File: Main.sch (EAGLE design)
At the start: 27 parts, among them U1 L298, U2 LM 1084 IT5,0, U3 LM 1084 IT3,3, U4 L298, X1 Motors, X3 Battery

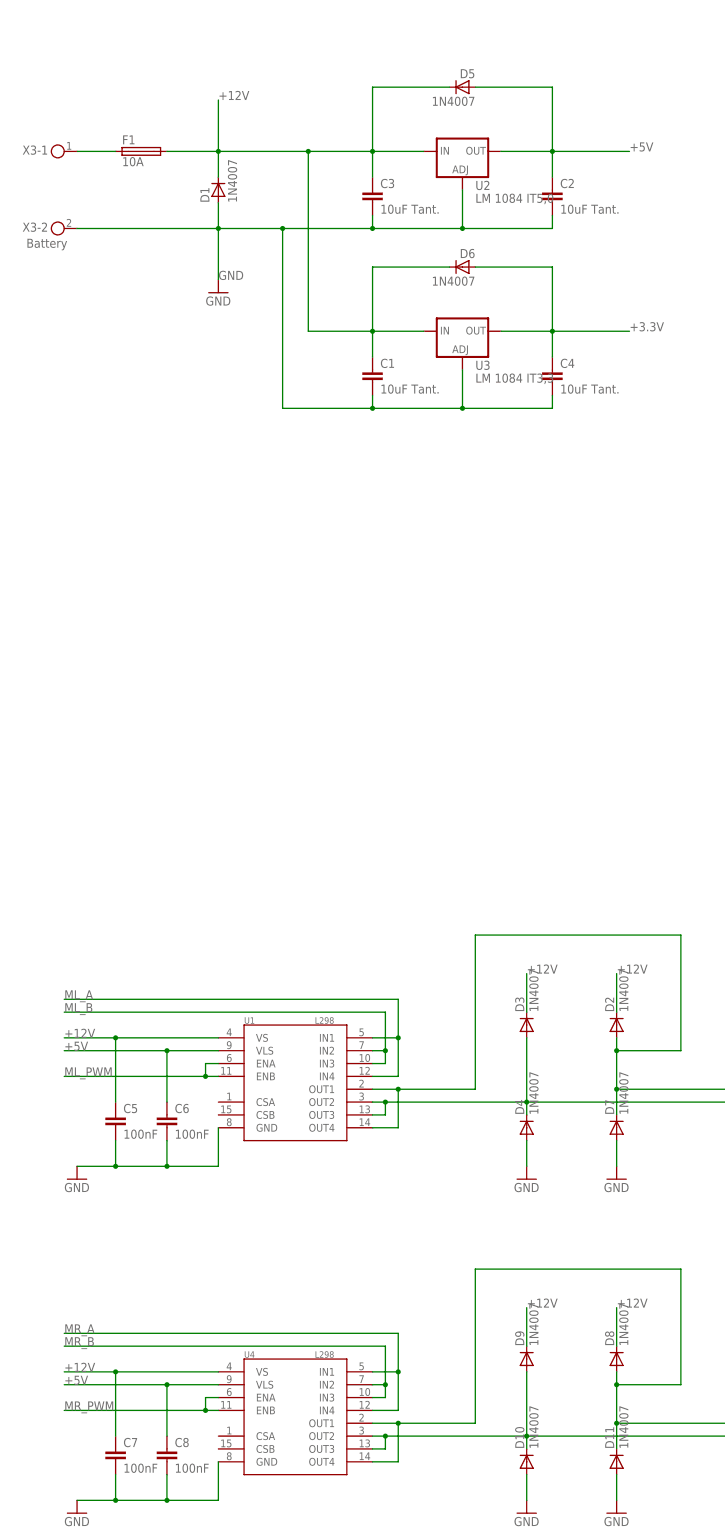
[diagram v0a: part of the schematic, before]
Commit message: better protection for reverse polarity
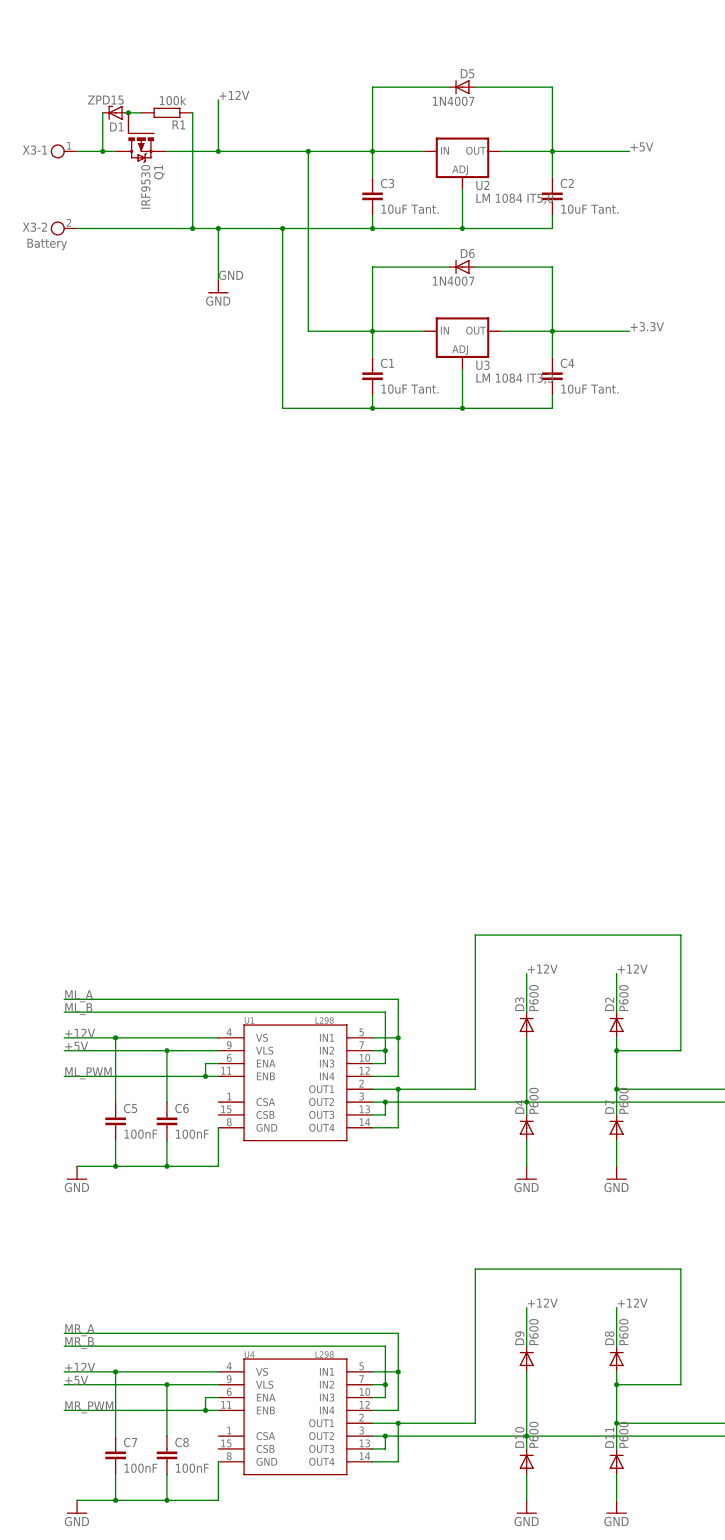
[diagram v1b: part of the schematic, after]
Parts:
- removed F1: 10A, fuse:FUSEBLANK_5X20MM
- added Q1: IRF9530, transistor-power:IRF9530
- added R1: 100k, resistor:R-EU_R0805
- D1: value 1N4007 -> ZPD15; device semicon-smd-ipc:D-MLL-41 -> diode:ZENER-DIODEDO35Z10
- D10, D11, D2, D3, D4, D7, D8, D9: value 1N4007 -> P600
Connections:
- new net N$2: D1.A, Q1.G, R1.2
- net +12V: now also Q1.S; no longer D1.C, F1.2
- net GND: now also R1.1; no longer D1.A
- net N$1: now also D1.C, Q1.D; no longer F1.1
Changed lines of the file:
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@@
 <part name="D6" library="semicon-smd-ipc" deviceset="D-" device="MLL-41" value="1N4007"/>
 <part name="C4" library="rcl" deviceset="C-EU" device="025-040X050" value="10uF Tant."/>
-<part name="D1" library="semicon-smd-ipc" deviceset="D-" device="MLL-41" value="1N4007"/>
-<part name="F1" library="fuse" deviceset="FUSE" device="BLANK_5X20MM" value="10A"/>
 <part name="FRAME1" library="frames" deviceset="DINA4_L" device="" value="Power"/>
 <part name="FRAME2" library="frames" deviceset="DINA4_L" device="" value="Motor"/>
@@
 <part name="SV1" library="con-lsta" deviceset="FE20-2" device="" value="Raspberry Pi B Plus Connector"/>
 <part name="GND4" library="supply1" deviceset="GND" device=""/>
-<part name="D2" library="diode" deviceset="P600" device="" value="1N4007"/>
-<part name="D3" library="diode" deviceset="P600" device="" value="1N4007"/>
-<part name="D4" library="diode" deviceset="P600" device="" value="1N4007"/>
-<part name="D7" library="diode" deviceset="P600" device="" value="1N4007"/>
+<part name="D2" library="diode" deviceset="P600" device="" value="P600"/>
+<part name="D3" library="diode" deviceset="P600" device="" value="P600"/>
+<part name="D4" library="diode" deviceset="P600" device="" value="P600"/>
+<part name="D7" library="diode" deviceset="P600" device="" value="P600"/>
 <part name="GND2" library="supply1" deviceset="GND" device=""/>
 <part name="GND5" library="supply1" deviceset="GND" device=""/>
@@
 <part name="C8" library="rcl" deviceset="C-EU" device="C0805" value="100nF"/>
 <part name="GND6" library="supply1" deviceset="GND" device=""/>
-<part name="D8" library="diode" deviceset="P600" device="" value="1N4007"/>
-<part name="D9" library="diode" deviceset="P600" device="" value="1N4007"/>
-<part name="D10" library="diode" deviceset="P600" device="" value="1N4007"/>
-<part name="D11" library="diode" deviceset="P600" device="" value="1N4007"/>
+<part name="D8" library="diode" deviceset="P600" device="" value="P600"/>
+<part name="D9" library="diode" deviceset="P600" device="" value="P600"/>
+<part name="D10" library="diode" deviceset="P600" device="" value="P600"/>
+<part name="D11" library="diode" deviceset="P600" device="" value="P600"/>
 <part name="GND7" library="supply1" deviceset="GND" device=""/>
 <part name="GND8" library="supply1" deviceset="GND" device=""/>
@@
 <part name="X3" library="con-ria-59" deviceset="AKL59-02" device="" value="Battery"/>
 <part name="X1" library="con-ria-59" deviceset="AKL59-08" device="" value="Motors"/>
+<part name="Q1" library="transistor-power" deviceset="IRF9530" device=""/>
+<part name="R1" library="resistor" deviceset="R-EU_" device="R0805" value="100k"/>
+<part name="D1" library="diode" deviceset="ZENER-DIODE" device="DO35Z10" value="ZPD15"/>
 </parts>
 <sheets>
@@
 <instance part="D6" gate="G$1" x="-411.48" y="317.5" rot="MR0"/>
 <instance part="C4" gate="G$1" x="-393.7" y="297.18"/>
-<instance part="D1" gate="G$1" x="-459.74" y="332.74" rot="R90"/>
-<instance part="F1" gate="G$1" x="-474.98" y="340.36"/>
 <instance part="FRAME1" gate="G$1" x="-513.08" y="213.36"/>
 <instance part="FRAME1" gate="G$2" x="-350.52" y="213.36"/>
@@
 <instance part="X1" gate="-7" x="-327.66" y="109.22"/>
 <instance part="X1" gate="-8" x="-327.66" y="104.14"/>
+<instance part="Q1" gate="G$1" x="-474.98" y="342.9" rot="R270"/>
+<instance part="R1" gate="G$1" x="-469.9" y="347.98" rot="R180"/>
+<instance part="D1" gate="G$1" x="-480.06" y="347.98" rot="R180"/>
 </instances>
 <busses>
@@
 <wire x1="-441.96" y1="304.8" x2="-441.96" y2="340.36" width="0.1524" layer="91"/>
 <junction x="-441.96" y="340.36"/>
-<pinref part="D1" gate="G$1" pin="C"/>
 <wire x1="-459.74" y1="340.36" x2="-441.96" y2="340.36" width="0.1524" layer="91"/>
-<wire x1="-459.74" y1="340.36" x2="-459.74" y2="335.28" width="0.1524" layer="91"/>
 <junction x="-459.74" y="340.36"/>
-<pinref part="F1" gate="G$1" pin="2"/>
 <wire x1="-469.9" y1="340.36" x2="-459.74" y2="340.36" width="0.1524" layer="91"/>
 <wire x1="-459.74" y1="340.36" x2="-459.74" y2="350.52" width="0.1524" layer="91"/>
@@
 <pinref part="C3" gate="G$1" pin="1"/>
 <wire x1="-429.26" y1="335.28" x2="-429.26" y2="340.36" width="0.1524" layer="91"/>
+<pinref part="Q1" gate="G$1" pin="S"/>
 </segment>
 <segment>
@@
 <net name="N$1" class="0">
 <segment>
-<pinref part="F1" gate="G$1" pin="1"/>
-<wire x1="-487.68" y1="340.36" x2="-480.06" y2="340.36" width="0.1524" layer="91"/>
+<wire x1="-487.68" y1="340.36" x2="-482.6" y2="340.36" width="0.1524" layer="91"/>
 <pinref part="X3" gate="-1" pin="1"/>
+<pinref part="Q1" gate="G$1" pin="D"/>
+<pinref part="D1" gate="G$1" pin="C"/>
+<wire x1="-482.6" y1="340.36" x2="-480.06" y2="340.36" width="0.1524" layer="91"/>
+<wire x1="-482.6" y1="347.98" x2="-482.6" y2="340.36" width="0.1524" layer="91"/>
+<junction x="-482.6" y="340.36"/>
 </segment>
 </net>
@@
 <wire x1="-447.04" y1="289.56" x2="-447.04" y2="325.12" width="0.1524" layer="91"/>
 <junction x="-447.04" y="325.12"/>
-<wire x1="-487.68" y1="325.12" x2="-459.74" y2="325.12" width="0.1524" layer="91"/>
+<wire x1="-487.68" y1="325.12" x2="-464.82" y2="325.12" width="0.1524" layer="91"/>
 <pinref part="C2" gate="G$1" pin="2"/>
+<wire x1="-464.82" y1="325.12" x2="-459.74" y2="325.12" width="0.1524" layer="91"/>
 <wire x1="-459.74" y1="325.12" x2="-447.04" y2="325.12" width="0.1524" layer="91"/>
 <wire x1="-393.7" y1="327.66" x2="-393.7" y2="325.12" width="0.1524" layer="91"/>
@@
 <wire x1="-393.7" y1="289.56" x2="-393.7" y2="292.1" width="0.1524" layer="91"/>
 <junction x="-459.74" y="325.12"/>
-<pinref part="D1" gate="G$1" pin="A"/>
-<wire x1="-459.74" y1="325.12" x2="-459.74" y2="330.2" width="0.1524" layer="91"/>
 <wire x1="-459.74" y1="325.12" x2="-459.74" y2="314.96" width="0.1524" layer="91"/>
 <label x="-459.74" y="314.96" size="1.778" layer="95"/>
@@
 <pinref part="GND1" gate="1" pin="GND"/>
 <pinref part="X3" gate="-2" pin="1"/>
+<pinref part="R1" gate="G$1" pin="1"/>
+<wire x1="-464.82" y1="347.98" x2="-464.82" y2="325.12" width="0.1524" layer="91"/>
+<junction x="-464.82" y="325.12"/>
 </segment>
 <segment>
@@
 </segment>
 </net>
+<net name="N$2" class="0">
+<segment>
+<pinref part="R1" gate="G$1" pin="2"/>
+<pinref part="Q1" gate="G$1" pin="G"/>
+<pinref part="D1" gate="G$1" pin="A"/>
+<junction x="-477.52" y="347.98"/>
+<wire x1="-477.52" y1="347.98" x2="-474.98" y2="347.98" width="0.1524" layer="91"/>
+</segment>
+</net>

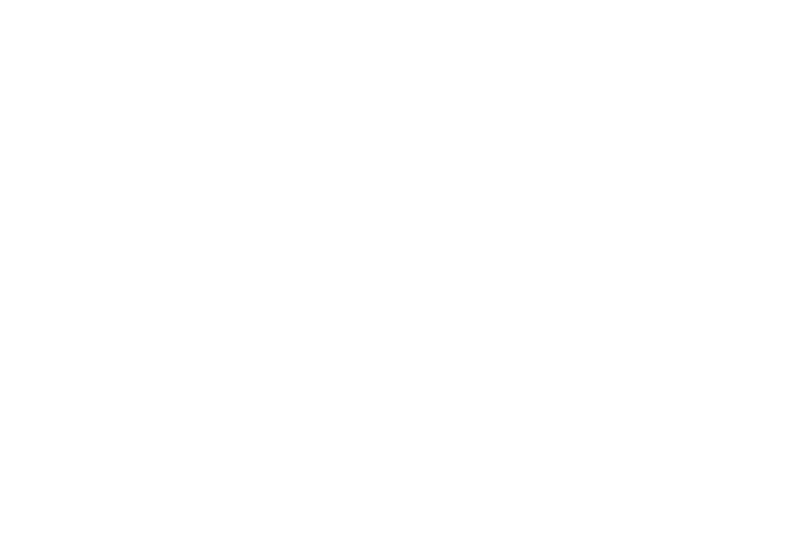
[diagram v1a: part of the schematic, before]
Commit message: added PIRs
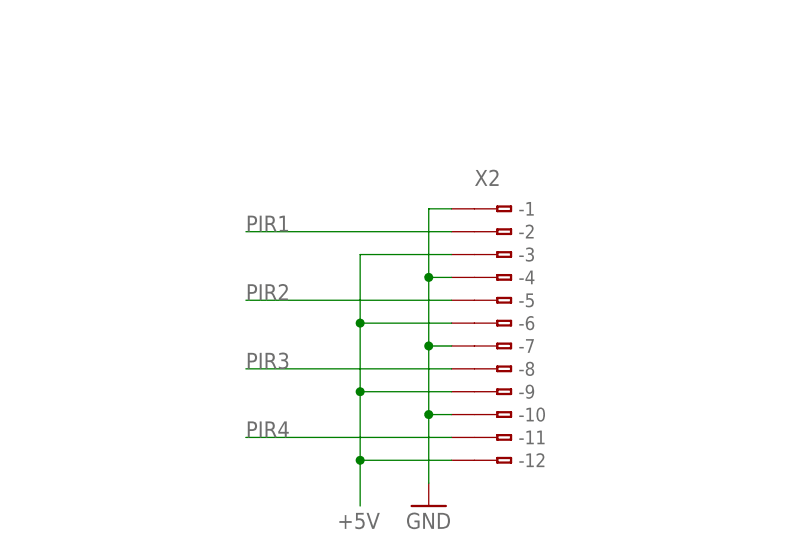
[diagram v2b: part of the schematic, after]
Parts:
- added X2: (no value), con-wago:233-512
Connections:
- new net PIR1: X2.B-2
- new net PIR2: X2.B-5
- new net PIR3: X2.B-8
- new net PIR4: X2.B-11
- net +5V: now also X2.B-12, X2.B-3, X2.B-6, X2.B-9
- net GND: now also X2.B-1, X2.B-10, X2.B-4, X2.B-7
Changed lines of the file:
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@@
 </variantdefs>
 <classes>
-<class number="0" name="default" width="0" drill="0">
+<class number="0" name="default" width="0.4064" drill="0">
+</class>
+<class number="1" name="10A" width="2.032" drill="0">
+</class>
+<class number="2" name="6A" width="1.016" drill="0">
 </class>
 </classes>
@@
 <part name="R1" library="resistor" deviceset="R-EU_" device="R0805" value="100k"/>
 <part name="D1" library="diode" deviceset="ZENER-DIODE" device="DO35Z10" value="ZPD15"/>
+<part name="X2" library="con-wago" deviceset="233-512" device=""/>
+<part name="GND9" library="supply1" deviceset="GND" device=""/>
 </parts>
 <sheets>
@@
 <instance part="R1" gate="G$1" x="-469.9" y="347.98" rot="R180"/>
 <instance part="D1" gate="G$1" x="-480.06" y="347.98" rot="R180"/>
+<instance part="X2" gate="G$1" x="-398.78" y="-68.58"/>
+<instance part="GND9" gate="1" x="-408.94" y="-88.9"/>
 </instances>
 <busses>
@@
 <wire x1="-469.9" y1="86.36" x2="-469.9" y2="96.52" width="0.1524" layer="91"/>
 <junction x="-469.9" y="96.52"/>
+</segment>
+<segment>
+<pinref part="X2" gate="G$1" pin="B-3"/>
+<wire x1="-406.4" y1="-60.96" x2="-416.56" y2="-60.96" width="0.1524" layer="91"/>
+<pinref part="X2" gate="G$1" pin="B-6"/>
+<wire x1="-406.4" y1="-68.58" x2="-416.56" y2="-68.58" width="0.1524" layer="91"/>
+<wire x1="-416.56" y1="-60.96" x2="-416.56" y2="-68.58" width="0.1524" layer="91"/>
+<junction x="-416.56" y="-68.58"/>
+<pinref part="X2" gate="G$1" pin="B-9"/>
+<wire x1="-406.4" y1="-76.2" x2="-416.56" y2="-76.2" width="0.1524" layer="91"/>
+<wire x1="-416.56" y1="-68.58" x2="-416.56" y2="-76.2" width="0.1524" layer="91"/>
+<junction x="-416.56" y="-76.2"/>
+<pinref part="X2" gate="G$1" pin="B-12"/>
+<wire x1="-406.4" y1="-83.82" x2="-416.56" y2="-83.82" width="0.1524" layer="91"/>
+<wire x1="-416.56" y1="-76.2" x2="-416.56" y2="-83.82" width="0.1524" layer="91"/>
+<junction x="-416.56" y="-83.82"/>
+<wire x1="-416.56" y1="-83.82" x2="-416.56" y2="-88.9" width="0.1524" layer="91"/>
+<label x="-419.1" y="-91.44" size="1.778" layer="95"/>
 </segment>
 </net>
@@
 </segment>
 </net>
-<net name="N$1" class="0">
+<net name="N$1" class="1">
 <segment>
 <wire x1="-487.68" y1="340.36" x2="-482.6" y2="340.36" width="0.1524" layer="91"/>
@@
 </segment>
 </net>
-<net name="GND" class="0">
+<net name="GND" class="1">
 <segment>
 <wire x1="-411.48" y1="289.56" x2="-393.7" y2="289.56" width="0.1524" layer="91"/>
@@
 <wire x1="-381" y1="73.66" x2="-381" y2="78.74" width="0.1524" layer="91"/>
 </segment>
+<segment>
+<pinref part="X2" gate="G$1" pin="B-1"/>
+<pinref part="GND9" gate="1" pin="GND"/>
+<wire x1="-406.4" y1="-55.88" x2="-408.94" y2="-55.88" width="0.1524" layer="91"/>
+<wire x1="-408.94" y1="-55.88" x2="-408.94" y2="-63.5" width="0.1524" layer="91"/>
+<pinref part="X2" gate="G$1" pin="B-4"/>
+<wire x1="-408.94" y1="-63.5" x2="-408.94" y2="-71.12" width="0.1524" layer="91"/>
+<wire x1="-408.94" y1="-71.12" x2="-408.94" y2="-78.74" width="0.1524" layer="91"/>
+<wire x1="-408.94" y1="-78.74" x2="-408.94" y2="-86.36" width="0.1524" layer="91"/>
+<wire x1="-406.4" y1="-63.5" x2="-408.94" y2="-63.5" width="0.1524" layer="91"/>
+<junction x="-408.94" y="-63.5"/>
+<pinref part="X2" gate="G$1" pin="B-7"/>
+<wire x1="-406.4" y1="-71.12" x2="-408.94" y2="-71.12" width="0.1524" layer="91"/>
+<junction x="-408.94" y="-71.12"/>
+<pinref part="X2" gate="G$1" pin="B-10"/>
+<wire x1="-406.4" y1="-78.74" x2="-408.94" y2="-78.74" width="0.1524" layer="91"/>
+<junction x="-408.94" y="-78.74"/>
+</segment>
 </net>
 <net name="ML_PWM" class="0">
@@
 </segment>
 </net>
-<net name="ML_OUT_B" class="0">
+<net name="ML_OUT_B" class="2">
 <segment>
 <pinref part="D3" gate="G$1" pin="A"/>
@@
 </segment>
 </net>
-<net name="ML_OUT_A" class="0">
+<net name="ML_OUT_A" class="2">
 <segment>
 <pinref part="D2" gate="G$1" pin="A"/>
@@
 </segment>
 </net>
-<net name="MR_OUT_A" class="0">
+<net name="MR_OUT_A" class="2">
 <segment>
 <pinref part="D8" gate="G$1" pin="A"/>
@@
 </segment>
 </net>
-<net name="MR_OUT_B" class="0">
+<net name="MR_OUT_B" class="2">
 <segment>
 <pinref part="D9" gate="G$1" pin="A"/>
@@
 </segment>
 </net>
+<net name="PIR1" class="0">
+<segment>
+<pinref part="X2" gate="G$1" pin="B-2"/>
+<wire x1="-406.4" y1="-58.42" x2="-429.26" y2="-58.42" width="0.1524" layer="91"/>
+<label x="-429.26" y="-58.42" size="1.778" layer="95"/>
+</segment>
+</net>
+<net name="PIR2" class="0">
+<segment>
+<pinref part="X2" gate="G$1" pin="B-5"/>
+<wire x1="-406.4" y1="-66.04" x2="-429.26" y2="-66.04" width="0.1524" layer="91"/>
+<label x="-429.26" y="-66.04" size="1.778" layer="95"/>
+</segment>
+</net>
+<net name="PIR3" class="0">
+<segment>
+<pinref part="X2" gate="G$1" pin="B-8"/>
+<wire x1="-406.4" y1="-73.66" x2="-429.26" y2="-73.66" width="0.1524" layer="91"/>
+<label x="-429.26" y="-73.66" size="1.778" layer="95"/>
+</segment>
+</net>
+<net name="PIR4" class="0">
+<segment>
+<pinref part="X2" gate="G$1" pin="B-11"/>
+<wire x1="-406.4" y1="-81.28" x2="-429.26" y2="-81.28" width="0.1524" layer="91"/>
+<label x="-429.26" y="-81.28" size="1.778" layer="95"/>
+</segment>
+</net>

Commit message: connections to RPI
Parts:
- X2: value (none) -> PIRs
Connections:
- new net N$10: SV1.26
- new net N$11: SV1.24
- new net N$12: SV1.22
- new net N$13: SV1.20
- new net N$14: SV1.18
- new net N$15: SV1.16
- new net N$17: SV1.12
- new net N$18: SV1.10
- new net N$19: SV1.8
- new net N$20: SV1.3
- new net N$21: SV1.5
- new net N$22: SV1.7
- new net N$23: SV1.9
- new net N$24: SV1.11
- new net N$25: SV1.13
- new net N$27: SV1.17
- new net N$28: SV1.19
- new net N$29: SV1.21
- new net N$3: SV1.14
- new net N$30: SV1.23
- new net N$31: SV1.25
- new net N$32: SV1.27
- new net N$38: SV1.39
- new net N$6: SV1.34
- new net N$8: SV1.30
- new net N$9: SV1.28
- net +5V: now also SV1.2, SV1.4
- net ML_A: now also SV1.37
- net ML_B: now also SV1.35
- net ML_PWM: now also SV1.33
- net MR_A: now also SV1.31
- net MR_B: now also SV1.29
- net MR_PWM: now also SV1.15
- net PIR1: now also SV1.40
- net PIR2: now also SV1.36
- net PIR3: now also SV1.38
- net PIR4: now also SV1.32

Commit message: some cleanup
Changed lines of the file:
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@@
 <instance part="GND3" gate="1" x="-487.68" y="137.16"/>
 <instance part="SV1" gate="G$1" x="-388.62" y="518.16"/>
-<instance part="GND4" gate="1" x="-370.84" y="495.3"/>
+<instance part="GND4" gate="1" x="-340.36" y="495.3"/>
 <instance part="D2" gate="G$1" x="-381" y="167.64" rot="R90"/>
 <instance part="D3" gate="G$1" x="-398.78" y="167.64" rot="R90"/>
@@
 </segment>
 <segment>
+<pinref part="SV1" gate="G$1" pin="2"/>
+<wire x1="-381" y1="492.76" x2="-375.92" y2="492.76" width="0.1524" layer="91"/>
+<wire x1="-363.22" y1="492.76" x2="-375.92" y2="492.76" width="0.1524" layer="91"/>
+<wire x1="-375.92" y1="492.76" x2="-375.92" y2="495.3" width="0.1524" layer="91"/>
+<junction x="-375.92" y="492.76"/>
 <pinref part="SV1" gate="G$1" pin="4"/>
-<pinref part="SV1" gate="G$1" pin="2"/>
-<wire x1="-381" y1="495.3" x2="-381" y2="492.76" width="0.1524" layer="91"/>
-<wire x1="-381" y1="492.76" x2="-381" y2="490.22" width="0.1524" layer="91"/>
-<junction x="-381" y="492.76"/>
-<wire x1="-381" y1="490.22" x2="-360.68" y2="490.22" width="0.1524" layer="91"/>
-<label x="-363.22" y="490.22" size="1.778" layer="95"/>
+<wire x1="-375.92" y1="495.3" x2="-381" y2="495.3" width="0.1524" layer="91"/>
+<label x="-363.22" y="492.76" size="1.778" layer="95"/>
 </segment>
 </net>
@@
 <pinref part="SV1" gate="G$1" pin="6"/>
 <pinref part="GND4" gate="1" pin="GND"/>
-<wire x1="-381" y1="497.84" x2="-370.84" y2="497.84" width="0.1524" layer="91"/>
+<wire x1="-381" y1="497.84" x2="-340.36" y2="497.84" width="0.1524" layer="91"/>
 </segment>
 <segment>
@@
 <label x="-355.6" y="500.38" size="1.778" layer="95"/>
 </segment>
-<segment>
-<wire x1="-421.64" y1="492.76" x2="-396.24" y2="492.76" width="0.1524" layer="91"/>
-<label x="-421.64" y="492.76" size="1.778" layer="95"/>
-</segment>
-</net>
+</net>

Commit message: fuses
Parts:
- removed C3: 10uF Tant., rcl:C-EU025-040X050
- added F1: PFRA 600, Sicherungselemente:PTC-SICHERUNG-2.50
- added F2: PTC194600-110, _hhn_PtcFuses_Siba_r500:SIBA194600
- added F3, F4, F5, F6: PTC194600-150, _hhn_PtcFuses_Siba_r500:SIBA194600
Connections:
- new net N$26: F4.2, X1-3.1
- new net N$34: F5.2, X1-5.1
- new net N$36: F6.2, X1-7.1
- new net N$4: F1.1, X3-1.1
- new net N$5: F2.1, SV1.2, SV1.4
- new net N$7: F3.2, X1-1.1
- net +12V: no longer C3.1
- net +5V: now also F2.2; no longer SV1.2, SV1.4
- net GND: no longer C3.2
- net ML_OUT_A: now also F3.1, F4.1; no longer X1-1.1, X1-3.1
- net MR_OUT_A: now also F5.1, F6.1; no longer X1-5.1, X1-7.1
- net N$1: now also F1.2; no longer X3-1.1
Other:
- moved on the sheet: C1, C2, C4, D1, D5, D6, Q1, R1, U2, U3, X1-1, X1-2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

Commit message: added 2 ultrasonic sensors
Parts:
- added R2, R4: 330, resistor:R-EU_R0805
- added R3, R5: 470, resistor:R-EU_R0805
- added X4: (no value), con-wago:233-508
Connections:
- removed net N$14: SV1.18
- removed net N$15: SV1.16
- removed net N$22: SV1.7
- removed net N$24: SV1.11
- new net N$16: R2.1, X4.B-3
- new net N$35: R4.1, X4.B-7
- new net USM_A_ECHO: R2.2, R3.1, SV1.11
- new net USM_A_TRIG: SV1.7, X4.B-2
- new net USM_B_ECHO: R4.2, R5.1, SV1.18
- new net USM_B_TRIG: SV1.16, X4.B-6
- net +5V: now also X4.B-1, X4.B-5
- net GND: now also R3.2, R5.2, X4.B-4, X4.B-8
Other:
- moved on the sheet: X2
